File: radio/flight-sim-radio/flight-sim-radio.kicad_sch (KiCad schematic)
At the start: 30 parts, among them J1 Conn_01x03, J2 Conn_01x09, J3 Conn_01x04, SW1 RS-08 300±150GF, SW2 RotaryEncoder_Switch, SW3 RotaryEncoder_Switch, U1 74LS148, U2 TM1637, U3 TM1637

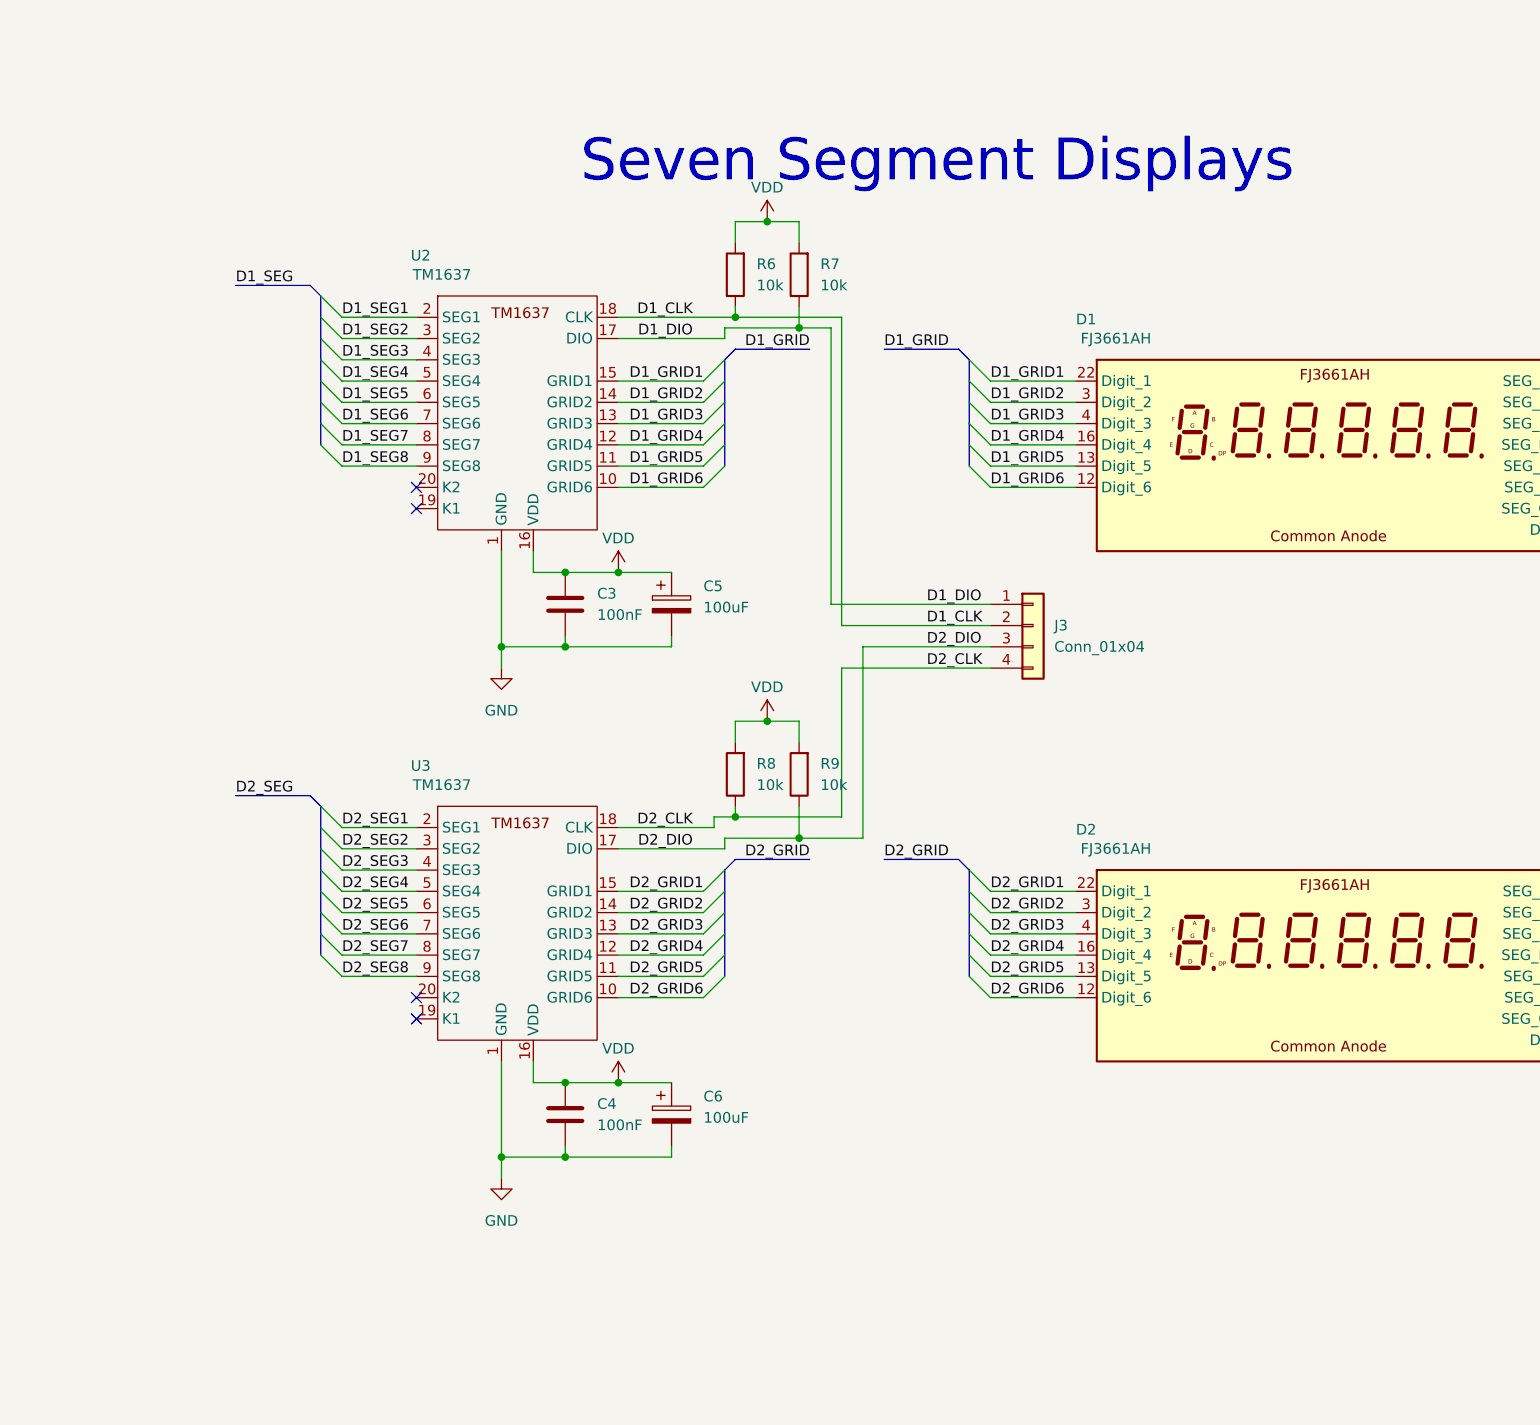
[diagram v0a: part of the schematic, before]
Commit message: Added new driver to schematic
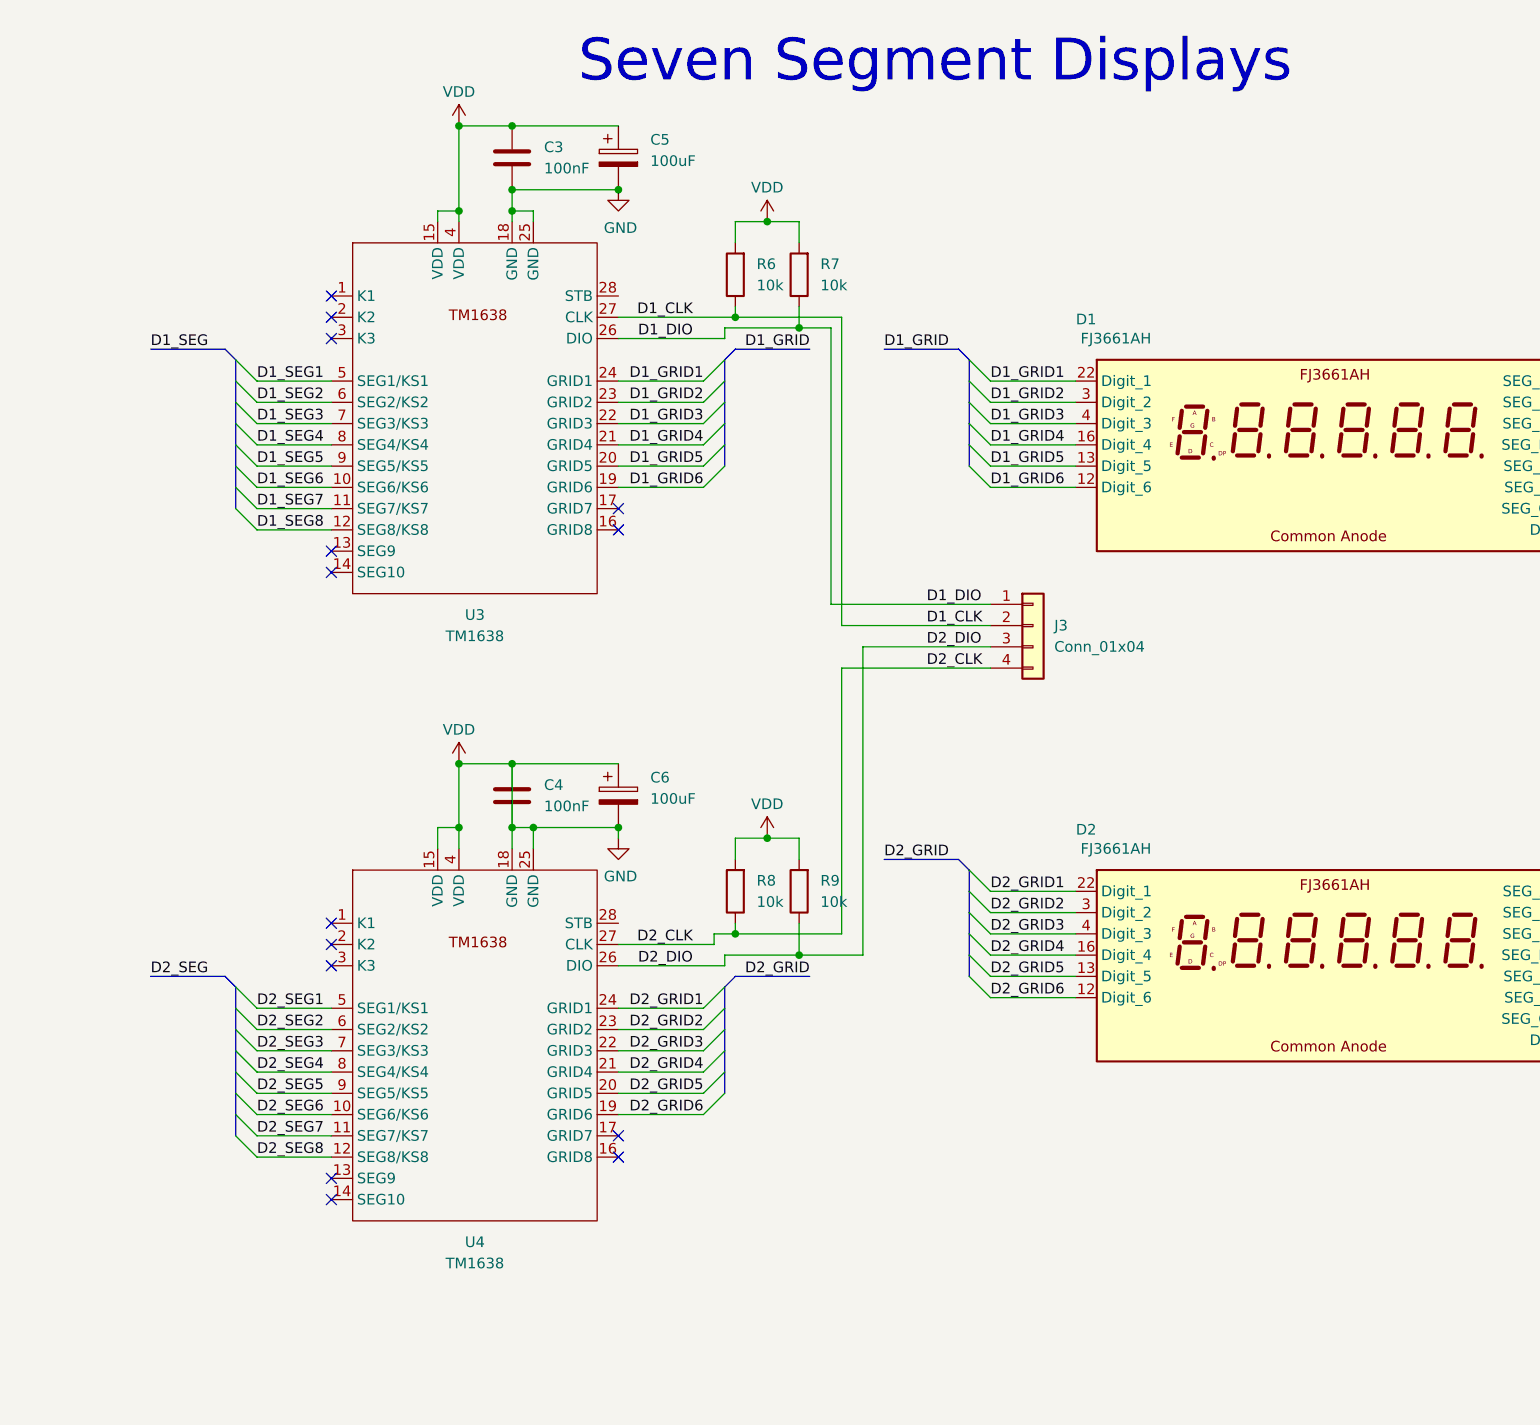
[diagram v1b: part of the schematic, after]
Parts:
- removed U2, U3: TM1637, Package_DIP:DIP-20_W7.62mm, symbol Radio_Components:TM1637
- added U3, U4: TM1638, radio_footprints:TM1638, symbol Radio_Components:TM1638
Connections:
- net VDD is gone; now on net GND: C1.1, C2.2, C3.1, C4.1, C5.1, C6.1, J1.2 (Pin_2), R6.2, R7.2, R8.2, R9.2, U1.16 (VCC)
- net D1_CLK: now also U3.27 (CLK)
- net D1_DIO: now also U3.26 (DIO)
- net D1_GRID1: now also U3.24 (GRID1)
- net D1_GRID2: now also U3.23 (GRID2)
- net D1_GRID3: now also U3.22 (GRID3)
- net D1_GRID4: now also U3.21 (GRID4)
- net D1_GRID5: now also U3.20 (GRID5)
- net D1_GRID6: now also U3.19 (GRID6)
- net D1_SEG1: now also U3.5 (SEG1/KS1)
- net D1_SEG2: now also U3.6 (SEG2/KS2)
- net D1_SEG3: now also U3.7 (SEG3/KS3)
- net D1_SEG4: now also U3.8 (SEG4/KS4)
- net D1_SEG5: now also U3.9 (SEG5/KS5)
- net D1_SEG6: now also U3.10 (SEG6/KS6)
- net D1_SEG7: now also U3.11 (SEG7/KS7)
- net D1_SEG8: now also U3.12 (SEG8/KS8)
- net D2_CLK: now also U4.27 (CLK)
- net D2_DIO: now also U4.26 (DIO)
- net D2_GRID1: now also U4.24 (GRID1)
- net D2_GRID2: now also U4.23 (GRID2)
- net D2_GRID3: now also U4.22 (GRID3)
- net D2_GRID4: now also U4.21 (GRID4)
- net D2_GRID5: now also U4.20 (GRID5)
- net D2_GRID6: now also U4.19 (GRID6)
- net D2_SEG1: now also U4.5 (SEG1/KS1)
- net D2_SEG2: now also U4.6 (SEG2/KS2)
- net D2_SEG3: now also U4.7 (SEG3/KS3)
- net D2_SEG4: now also U4.8 (SEG4/KS4)
- net D2_SEG5: now also U4.9 (SEG5/KS5)
- net D2_SEG6: now also U4.10 (SEG6/KS6)
- net D2_SEG7: now also U4.11 (SEG7/KS7)
- net D2_SEG8: now also U4.12 (SEG8/KS8)
- net GND: now also U3.15 (VDD), U3.18 (GND), U3.25 (GND), U3.4 (VDD), U4.15 (VDD), U4.18 (GND), U4.25 (GND), U4.4 (VDD)
- no-connect marks 8 -> 18
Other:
- moved on the sheet: R8, R9

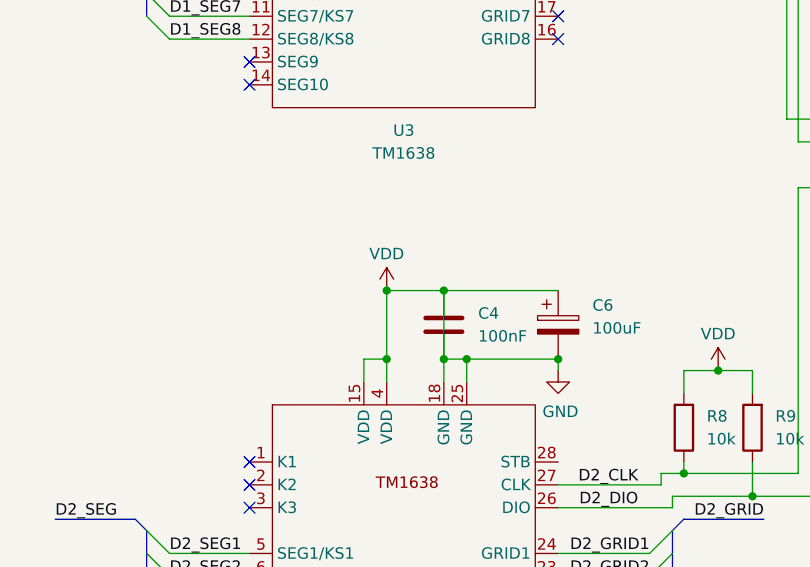
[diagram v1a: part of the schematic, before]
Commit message: First driver layed out
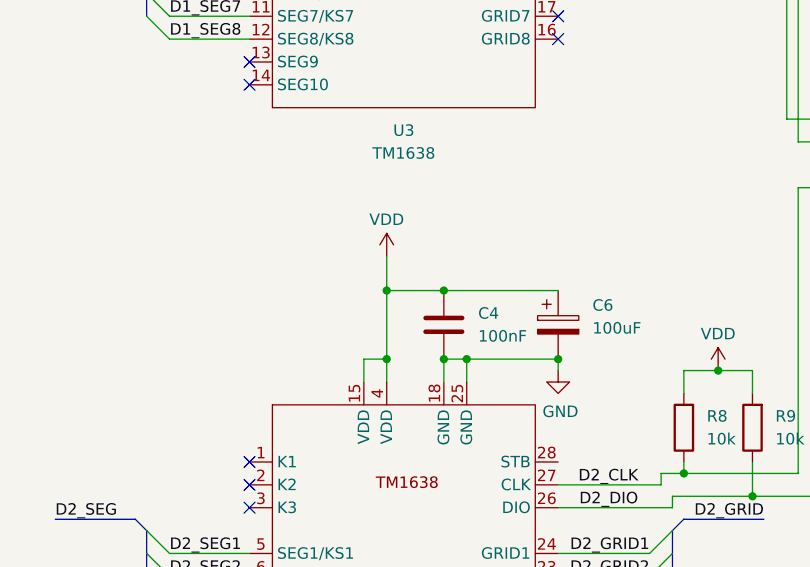
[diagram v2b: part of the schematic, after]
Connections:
- net GND: no longer C1.1, C2.2, C3.1, C4.1, C5.1, C6.1, J1.2 (Pin_2), R6.2, R7.2, R8.2, R9.2, U1.16 (VCC), U3.15 (VDD), U3.4 (VDD), U4.15 (VDD), U4.4 (VDD)
- new net VDD: C1.1, C2.2, C3.1, C4.1, C5.1, C6.1, J1.2 (Pin_2), R6.2, R7.2, R8.2, R9.2, U1.16 (VCC), U3.15 (VDD), U3.4 (VDD), U4.15 (VDD), U4.4 (VDD)
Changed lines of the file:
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@@
 	(wire
 		(pts
-			(xy 251.46 116.84) (xy 251.46 124.46)
-		)
-		(stroke
-			(width 0)
-			(type default)
-		)
-	)
-	(wire
-		(pts
 			(xy 220.98 148.59) (xy 229.87 148.59)
 		)
@@
 	(wire
 		(pts
+			(xy 245.11 113.03) (xy 245.11 116.84)
+		)
+		(stroke
+			(width 0)
+			(type default)
+		)
+	)
+	(wire
+		(pts
 			(xy 251.46 40.64) (xy 245.11 40.64)
 		)
@@
 	(symbol
 		(lib_id "power:VDD")
-		(at 245.11 116.84 0)
+		(at 245.11 113.03 0)
 		(unit 1)
 		(exclude_from_sim no)
@@
 		(dnp no)
 		(property "Reference" "#PWR012"
-			(at 245.11 120.65 0)
+			(at 245.11 116.84 0)
 			(effects
 				(font
@@
 		)
 		(property "Value" "VDD"
-			(at 245.11 112.776 0)
+			(at 245.11 108.966 0)
 			(effects
 				(font
@@
 		)
 		(property "Footprint" ""
-			(at 245.11 116.84 0)
+			(at 245.11 113.03 0)
 			(effects
 				(font
@@
 		)
 		(property "Datasheet" ""
-			(at 245.11 116.84 0)
+			(at 245.11 113.03 0)
 			(effects
 				(font
@@
 		)
 		(property "Description" "Power symbol creates a global label with name \"VDD\""
-			(at 245.11 116.84 0)
+			(at 245.11 113.03 0)
 			(effects
 				(font

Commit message: PCB complete
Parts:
- removed R8, R9: 10k, Resistor_THT:R_Axial_DIN0207_L6.3mm_D2.5mm_P10.16mm_Horizontal, symbol Device:R
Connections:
- net D2_STB: now reaches U4.28 (STB)
- net D2_STB: now also J3.4 (Pin_4)
- net D1_STB: now reaches U3.28 (STB)
- net D1_STB: now also J3.3 (Pin_3)
- net D1_CLK renamed D_CLK
- net D_CLK: now also R7.1, U4.27 (CLK); no longer R6.1
- net D1_DIO renamed D_DIO
- net D_DIO: now also R6.1, U4.26 (DIO); no longer R7.1
- removed net D2_CLK: J3.4 (Pin_4), U4.27 (CLK)
- removed net D2_DIO: J3.3 (Pin_3), U4.26 (DIO)
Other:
- moved on the sheet: C3, C4, C5, C6, D1, D2, J3, U3, U4
